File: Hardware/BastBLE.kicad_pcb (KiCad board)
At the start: 2 copper layers, 50.8 x 22.9 mm, 39 parts, among them J1 Conn_Battery, J2 SWD, J3 Conn_left, J4 Conn_right, P1 USB_C_Plug_USB2.0, Q1 DMG3415U-7, SW1 RESET, U1 AP2112K-3.3, U2 E73-2G4M08S1C, U3 MCP73831-2-OT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

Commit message: change routeo
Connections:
- U2 pad 10: /VBAT -> /D9
- U2 pad 12: /D9 -> /VBAT
- U2 pad 14: /TX -> /D12
- U2 pad 15: /A3 -> /D13
- U2 pad 16: /RX -> /A5
- U2 pad 17: /D13 -> /A3
- U2 pad 18: /A2 -> /D11
- U2 pad 22: /D12 -> /A2
- U2 pad 38: /D11 -> /D10
- U2 pad 41: /D10 -> /RX
- U2 pad 43: /D6 -> /TX
- U2 pad 8: /A5 -> /D6
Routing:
- net /SDA: track 0.00 -> 39.4 mm, vias 0 -> 1
- net /A4: track 0.00 -> 38.5 mm, vias 0 -> 1
- net /QSPI_DATA2: track 0.00 -> 27.0 mm, vias 0 -> 1
- net /SCK: track 0.00 -> 26.3 mm, vias 0 -> 1
- net /QSPI_CS: track 0.00 -> 25.7 mm, vias 0 -> 1
- net /A2: track 0.00 -> 25.1 mm
- net /A5: track 0.00 -> 19.4 mm
- net /MOSI: track 0.00 -> 18.9 mm
- net /SCL: track 0.00 -> 15.7 mm, vias 0 -> 1
- net /D5: track 0.00 -> 13.0 mm
- net /RX: track 0.00 -> 12.4 mm
- net /TX: track 0.00 -> 11.4 mm
- net /MISO: track 0.00 -> 9.03 mm
- net /D9: track 0.00 -> 7.10 mm
- net /D6: track 0.00 -> 6.31 mm
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
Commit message: routeo D
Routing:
- net /D10: track 0.00 -> 25.4 mm, vias 0 -> 1
- net /D11: track 0.00 -> 24.7 mm, vias 0 -> 1
- net /D12: track 0.00 -> 23.1 mm
- net /D13: track 0.00 -> 18.2 mm, vias 0 -> 1
- net VBUS: track 0.00 -> 17.0 mm, vias 0 -> 2
- net +BATT: track 1.92 -> 12.4 mm
- net /EN: track 0.00 -> 7.13 mm
- net /SCL: track 15.7 -> 19.8 mm
- net /A4: track 38.5 -> 40.8 mm
- net /SCK: track 26.3 -> 27.0 mm

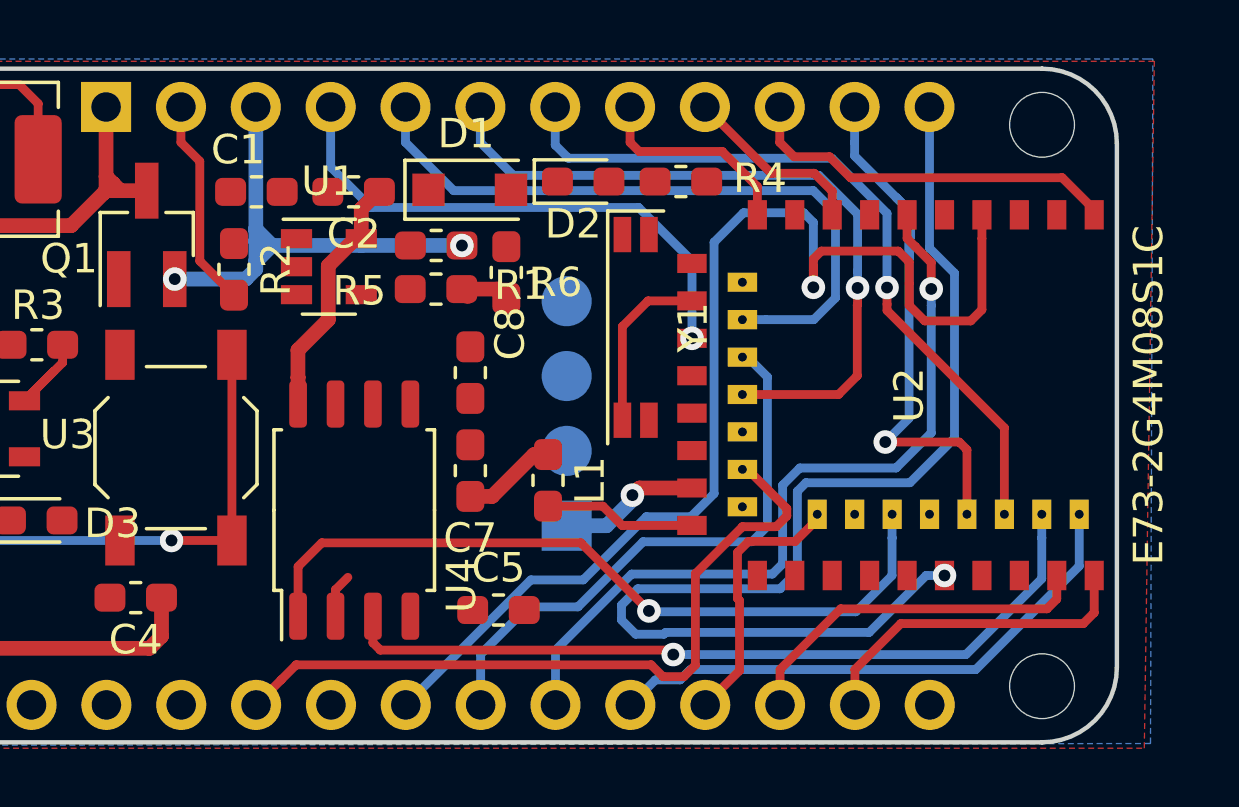
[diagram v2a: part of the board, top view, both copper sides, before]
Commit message: chenge analog signals routeo
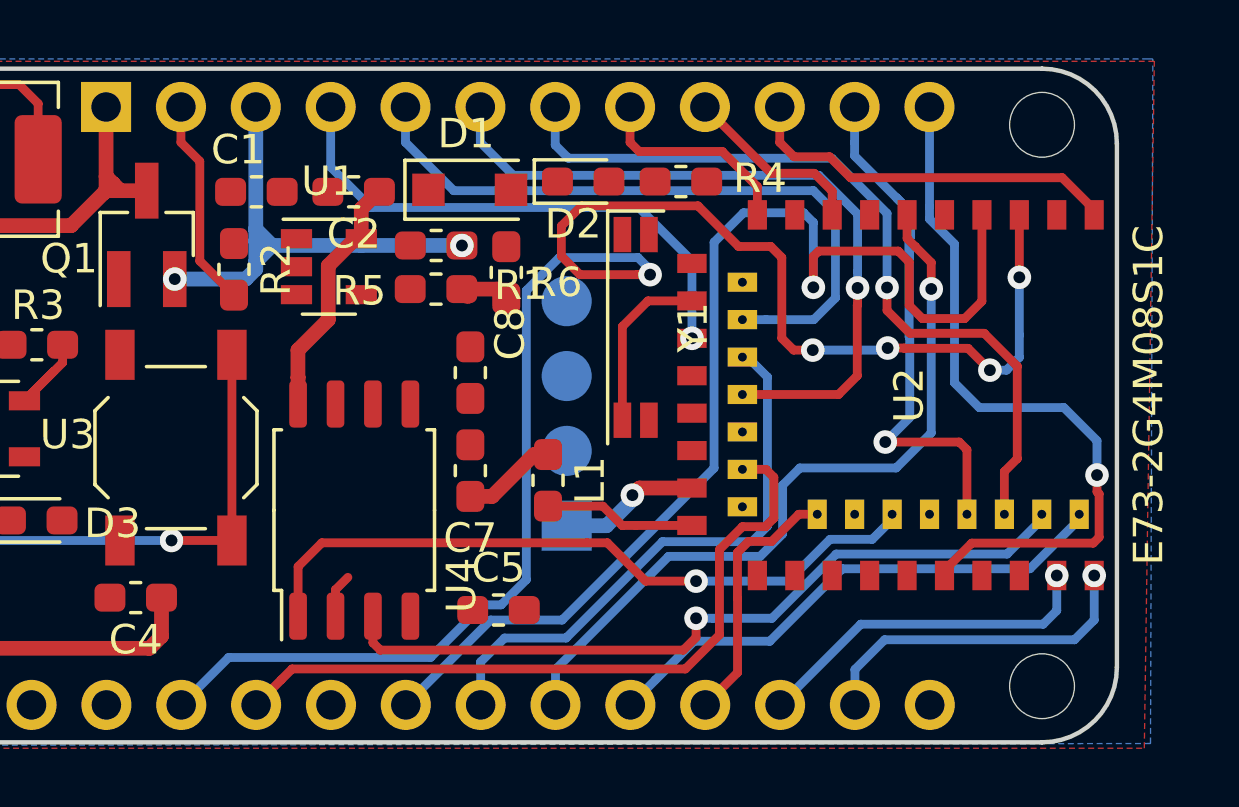
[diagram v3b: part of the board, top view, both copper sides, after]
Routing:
- net /A1: track 0.00 -> 57.4 mm, vias 0 -> 5
- net /SDA: track 39.3 -> 24.6 mm
- net /QSPI_CS: track 25.7 -> 23.8 mm
- net /D10: track 25.4 -> 27.2 mm
- net /A4: track 40.8 -> 39.4 mm
- net /SCK: track 27.0 -> 26.0 mm
- net /MOSI: track 18.9 -> 18.0 mm
- net /QSPI_DATA2: track 27.0 -> 26.1 mm
- net /A2: track 25.1 -> 24.5 mm
- net /RX: track 12.4 -> 11.9 mm, vias 0 -> 1
- net /TX: track 11.4 -> 11.5 mm, vias 0 -> 1

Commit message: A0 rf
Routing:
- net /A0: track 0.00 -> 31.5 mm
- net /A4: track 39.4 -> 44.3 mm
- net /D12: track 23.1 -> 27.8 mm
- net /SCL: track 19.8 -> 16.3 mm
- net /D11: track 24.7 -> 27.3 mm
- net /A1: track 57.4 -> 58.0 mm, vias 5 -> 3

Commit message: erase traces, add note
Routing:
- net /A1: track 58.0 -> 0.00 mm, vias 3 -> 0
- net /A4: track 44.3 -> 0.00 mm, vias 1 -> 0
- net +3V3: track 35.0 -> 0.00 mm, vias 1 -> 0
- net /A0: track 31.5 -> 0.00 mm
- net /D12: track 27.8 -> 0.00 mm
- net /D10: track 27.7 -> 0.00 mm, vias 1 -> 0
- net /D11: track 27.3 -> 0.00 mm, vias 1 -> 0
- net /QSPI_DATA2: track 26.1 -> 0.00 mm, vias 1 -> 0
- net /SCK: track 26.0 -> 0.00 mm, vias 1 -> 0
- net /RST: track 25.7 -> 0.00 mm, vias 1 -> 0
- net /A2: track 24.5 -> 0.00 mm
- net /SDA: track 24.3 -> 0.00 mm, vias 1 -> 0
- net /QSPI_CS: track 23.8 -> 0.00 mm, vias 1 -> 0
- net /A5: track 19.3 -> 0.00 mm
- net /D13: track 18.1 -> 0.00 mm, vias 1 -> 0
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
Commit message: add crystal and fix analogs
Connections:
- U2 pad 10: /D9 -> /A3
- U2 pad 15: /D13 -> /A2
- U2 pad 16: /A5 -> /D6
- U2 pad 17: /A3 -> /D9
- U2 pad 22: /A2 -> /D13
- U2 pad 8: /D6 -> /A5
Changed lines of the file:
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@@
-(kicad_pcb (version 20171130) (host pcbnew "(5.1.5)-3")
+(kicad_pcb (version 20171130) (host pcbnew "(5.1.5-0-10_14)")
   (general
     (thickness 1.6)
@@
   (net 42 /D-)
   (net 43 /RST)
-  (net 44 "Net-(U2-Pad11)")
-  (net 45 "Net-(U2-Pad13)")
-  (net 46 /D13)
-  (net 47 "Net-(L1-Pad2)")
-  (net 48 /D11)
-  (net 49 /D9)
-  (net 50 /D12)
+  (net 44 /D13)
+  (net 45 "Net-(L1-Pad2)")
+  (net 46 /D11)
+  (net 47 /D9)
+  (net 48 /D12)
+  (net 49 "Net-(C9-Pad1)")
+  (net 50 "Net-(C10-Pad1)")
   (net_class Default "This is the default net class."
     (clearance 0.2)
@@
     (add_net GND)
     (add_net "Net-(C1-Pad1)")
+    (add_net "Net-(C10-Pad1)")
+    (add_net "Net-(C9-Pad1)")
     (add_net "Net-(D2-Pad2)")
     (add_net "Net-(D3-Pad1)")
@@
     (add_net "Net-(R7-Pad2)")
     (add_net "Net-(U1-Pad4)")
-    (add_net "Net-(U2-Pad11)")
-    (add_net "Net-(U2-Pad13)")
   )
   (net_class VCC ""
@@
     (fp_line (start -0.8 0.4) (end -0.8 -0.4) (layer F.Fab) (width 0.1))
     (pad 2 smd roundrect (at 0.875 0 270) (size 1.05 0.95) (layers F.Cu F.Paste F.Mask) (roundrect_rratio 0.25)
-      (net 47 "Net-(L1-Pad2)"))
+      (net 45 "Net-(L1-Pad2)"))
     (pad 1 smd roundrect (at -0.875 0 270) (size 1.05 0.95) (layers F.Cu F.Paste F.Mask) (roundrect_rratio 0.25)
       (net 15 +3V3))
@@
       (net 6 /MISO))
     (pad 10 smd rect (at 2.6 -6.119) (size 0.65 1) (layers F.Cu F.Paste F.Mask)
-      (net 49 /D9))
+      (net 11 /A3))
     (pad 9 smd rect (at 3.87 -6.119) (size 0.65 1) (layers F.Cu F.Paste F.Mask)
       (net 20 /AREF))
     (pad 8 smd rect (at 5.14 -6.119) (size 0.65 1) (layers F.Cu F.Paste F.Mask)
-      (net 38 /D6))
+      (net 9 /A5))
     (pad 7 smd rect (at 6.41 -6.119) (size 0.65 1) (layers F.Cu F.Paste F.Mask)
       (net 14 /A0))
@@
       (net 15 +3V3))
     (pad 11 smd rect (at 0.381 -4.47 90) (size 0.65 1) (layers F.Cu F.Paste F.Mask)
-      (net 44 "Net-(U2-Pad11)"))
+      (net 49 "Net-(C9-Pad1)"))
     (pad 21 smd rect (at 0.381 1.88 90) (size 0.65 1) (layers F.Cu F.Paste F.Mask)
       (net 2 GND))
     (pad 13 smd rect (at 0.381 -3.2 90) (size 0.65 1) (layers F.Cu F.Paste F.Mask)
-      (net 45 "Net-(U2-Pad13)"))
+      (net 50 "Net-(C10-Pad1)"))
     (pad 15 smd rect (at 0.381 -1.93 90) (size 0.65 1) (layers F.Cu F.Paste F.Mask)
-      (net 46 /D13))
+      (net 12 /A2))
     (pad 17 smd rect (at 0.381 -0.66 90) (size 0.65 1) (layers F.Cu F.Paste F.Mask)
-      (net 11 /A3))
+      (net 47 /D9))
     (pad 25 smd rect (at 0.381 4.42 90) (size 0.65 1) (layers F.Cu F.Paste F.Mask)
-      (net 47 "Net-(L1-Pad2)"))
+      (net 45 "Net-(L1-Pad2)"))
     (pad 19 smd rect (at 0.381 0.61 90) (size 0.65 1) (layers F.Cu F.Paste F.Mask)
       (net 15 +3V3))
@@
       (net 7 /MOSI))
     (pad 14 thru_hole rect (at 2.092 -2.563 90) (size 0.65 1) (drill 0.3) (layers *.Cu *.Mask)
-      (net 50 /D12))
+      (net 48 /D12))
     (pad 12 thru_hole rect (at 2.092 -3.833 90) (size 0.65 1) (drill 0.3) (layers *.Cu *.Mask)
       (net 25 /VBAT))
@@
       (net 30 /QSPI_DATA3))
     (pad 16 thru_hole rect (at 2.092 -1.293 90) (size 0.65 1) (drill 0.3) (layers *.Cu *.Mask)
-      (net 9 /A5))
+      (net 38 /D6))
     (pad 22 thru_hole rect (at 2.092 2.517 90) (size 0.65 1) (drill 0.3) (layers *.Cu *.Mask)
-      (net 12 /A2))
+      (net 44 /D13))
     (pad 24 thru_hole rect (at 2.092 3.787 90) (size 0.65 1) (drill 0.3) (layers *.Cu *.Mask)
       (net 2 GND))
     (pad 18 thru_hole rect (at 2.092 -0.023 90) (size 0.65 1) (drill 0.3) (layers *.Cu *.Mask)
-      (net 48 /D11))
+      (net 46 /D11))
   )
   (module Diode_SMD:D_SOD-123F (layer F.Cu)
@@
       (net 3 VBUS))
     (pad 4 thru_hole oval (at 0 -7.62 270) (size 1.7 1.7) (drill 1) (layers *.Cu *.Mask)
-      (net 46 /D13))
+      (net 44 /D13))
     (pad 5 thru_hole oval (at 0 -10.16 270) (size 1.7 1.7) (drill 1) (layers *.Cu *.Mask)
-      (net 50 /D12))
+      (net 48 /D12))
     (pad 6 thru_hole oval (at 0 -12.7 270) (size 1.7 1.7) (drill 1) (layers *.Cu *.Mask)
-      (net 48 /D11))
+      (net 46 /D11))
     (pad 7 thru_hole oval (at 0 -15.24 270) (size 1.7 1.7) (drill 1) (layers *.Cu *.Mask)
       (net 39 /D10))
     (pad 8 thru_hole oval (at 0 -17.78 270) (size 1.7 1.7) (drill 1) (layers *.Cu *.Mask)
-      (net 49 /D9))
+      (net 47 /D9))
     (pad 9 thru_hole oval (at 0 -20.32 270) (size 1.7 1.7) (drill 1) (layers *.Cu *.Mask)
       (net 38 /D6))
@@
     (fp_line (start 4 -1) (end -4 -1) (layer F.CrtYd) (width 0.05))
     (pad 1 smd rect (at -3.15 0.45 270) (size 1.2 0.6) (layers F.Cu F.Paste F.Mask)
-      (net 44 "Net-(U2-Pad11)"))
+      (net 49 "Net-(C9-Pad1)"))
     (pad 2 smd rect (at 3.15 0.45 270) (size 1.2 0.6) (layers F.Cu F.Paste F.Mask)
-      (net 45 "Net-(U2-Pad13)"))
+      (net 50 "Net-(C10-Pad1)"))
     (pad 3 smd rect (at 3.15 -0.45 270) (size 1.2 0.6) (layers F.Cu F.Paste F.Mask))
     (pad 4 smd rect (at -3.15 -0.45 270) (size 1.2 0.6) (layers F.Cu F.Paste F.Mask))

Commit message: add footprint and netlist
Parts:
- added C10: 22pF, Capacitor_SMD:C_0603_1608Metric_Pad1.05x0.95mm_HandSolder, F.Cu at (162.4, 60.7)
- added C9: 22pF, Capacitor_SMD:C_0603_1608Metric_Pad1.05x0.95mm_HandSolder, F.Cu at (148.8, 73.0)
- D2, D3: footprint LED_SMD:LED_0603_1608Metric_Pad1.05x0.95mm_HandSolder -> LED_SMD:LED_0805_2012Metric
- J2: moved to F.Cu
- Q1: footprint Package_TO_SOT_SMD:SOT-23_Handsoldering -> Package_TO_SOT_SMD:SOT-23
- Y1: footprint Crystal:Crystal_SMD_SeikoEpson_MC146-4Pin_6.7x1.5mm -> Crystal:Crystal_SMD_3215-2Pin_3.2x1.5mm
- moved C6 43.2 mm to (157.7, 63.2)
- moved J2 43.0 mm to (134.2, 61.8)
- moved C3 39.5 mm to (158.0, 60.7), turned to 0 degrees
- moved R7 37.3 mm to (161.9, 68.2), turned to 0 degrees
- moved D3 34.5 mm to (153.3, 64.3)
- moved C4 33.3 mm to (153.2, 67.1), turned to 0 degrees
- moved SW1 31.5 mm to (141.2, 63.0), turned to 0 degrees
- moved C5 30.3 mm to (148.8, 70.5)
- moved Y1 29.3 mm to (148.9, 63.7), turned to 0 degrees
- moved C7 29.2 mm to (157.7, 65.7), turned to 0 degrees
- moved R3 27.8 mm to (157.6, 68.2), turned to 0 degrees
- moved R9 27.1 mm to (153.1, 77.1), turned to 0 degrees
- moved R8 26.8 mm to (157.5, 73.3), turned to 0 degrees
- moved U4 25.9 mm to (137.0, 75.1), turned to 0 degrees
- moved D1 25.3 mm to (148.8, 61.1)
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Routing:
- net +BATT: track 1.92 -> 0.00 mm
- net Net-(D3-Pad1): track 1.57 -> 0.00 mm
- net Net-(P1-PadA5): track 3.46 -> 2.87 mm

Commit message: fix components
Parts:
- C5, J2, U4: moved to B.Cu
- moved J2 42.8 mm to (160.6, 95.5)
- moved R1 40.5 mm to (136.4, 94.5), turned to 90 degrees
- moved C1 38.5 mm to (139.2, 96.4)
- moved C7 38.5 mm to (139.1, 99.4), turned to 180 degrees
- moved SW1 36.5 mm to (154.4, 97.0)
- moved C3 34.8 mm to (147.1, 93.8), turned to 270 degrees
- moved D1 34.6 mm to (139.7, 94.5)
- moved D3 33.2 mm to (148.9, 97.2), turned to 90 degrees
- moved R3 32.7 mm to (144.1, 98.0)
- moved R7 32.6 mm to (147.2, 97.3), turned to 90 degrees
- moved C10 30.8 mm to (160.0, 91.4), turned to 180 degrees
- moved C5 30.8 mm to (159.1, 99.5)
- moved C4 30.5 mm to (160.8, 96.6)
- moved R2 29.3 mm to (139.2, 97.9)
- moved Y1 27.8 mm to (160.9, 88.7), turned to 90 degrees
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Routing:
- net Net-(P1-PadA5): track 2.87 -> 1.87 mm
